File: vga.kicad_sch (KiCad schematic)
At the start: 48 parts

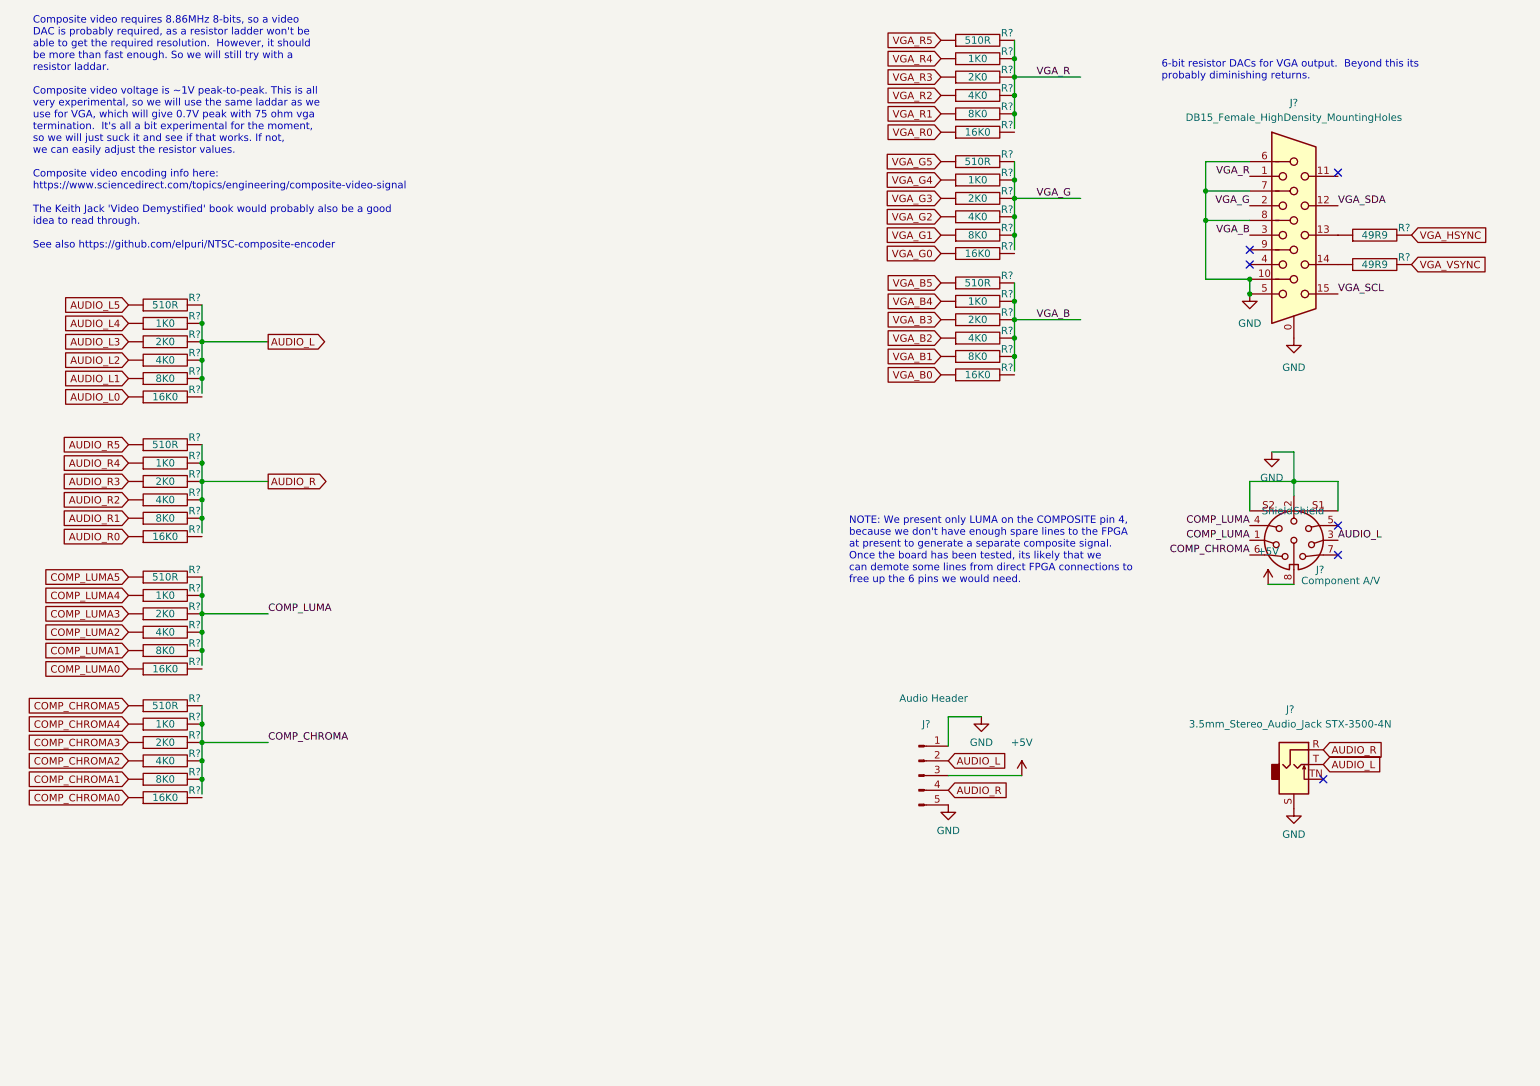
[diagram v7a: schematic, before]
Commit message: beautify the schematics, especially the title-page
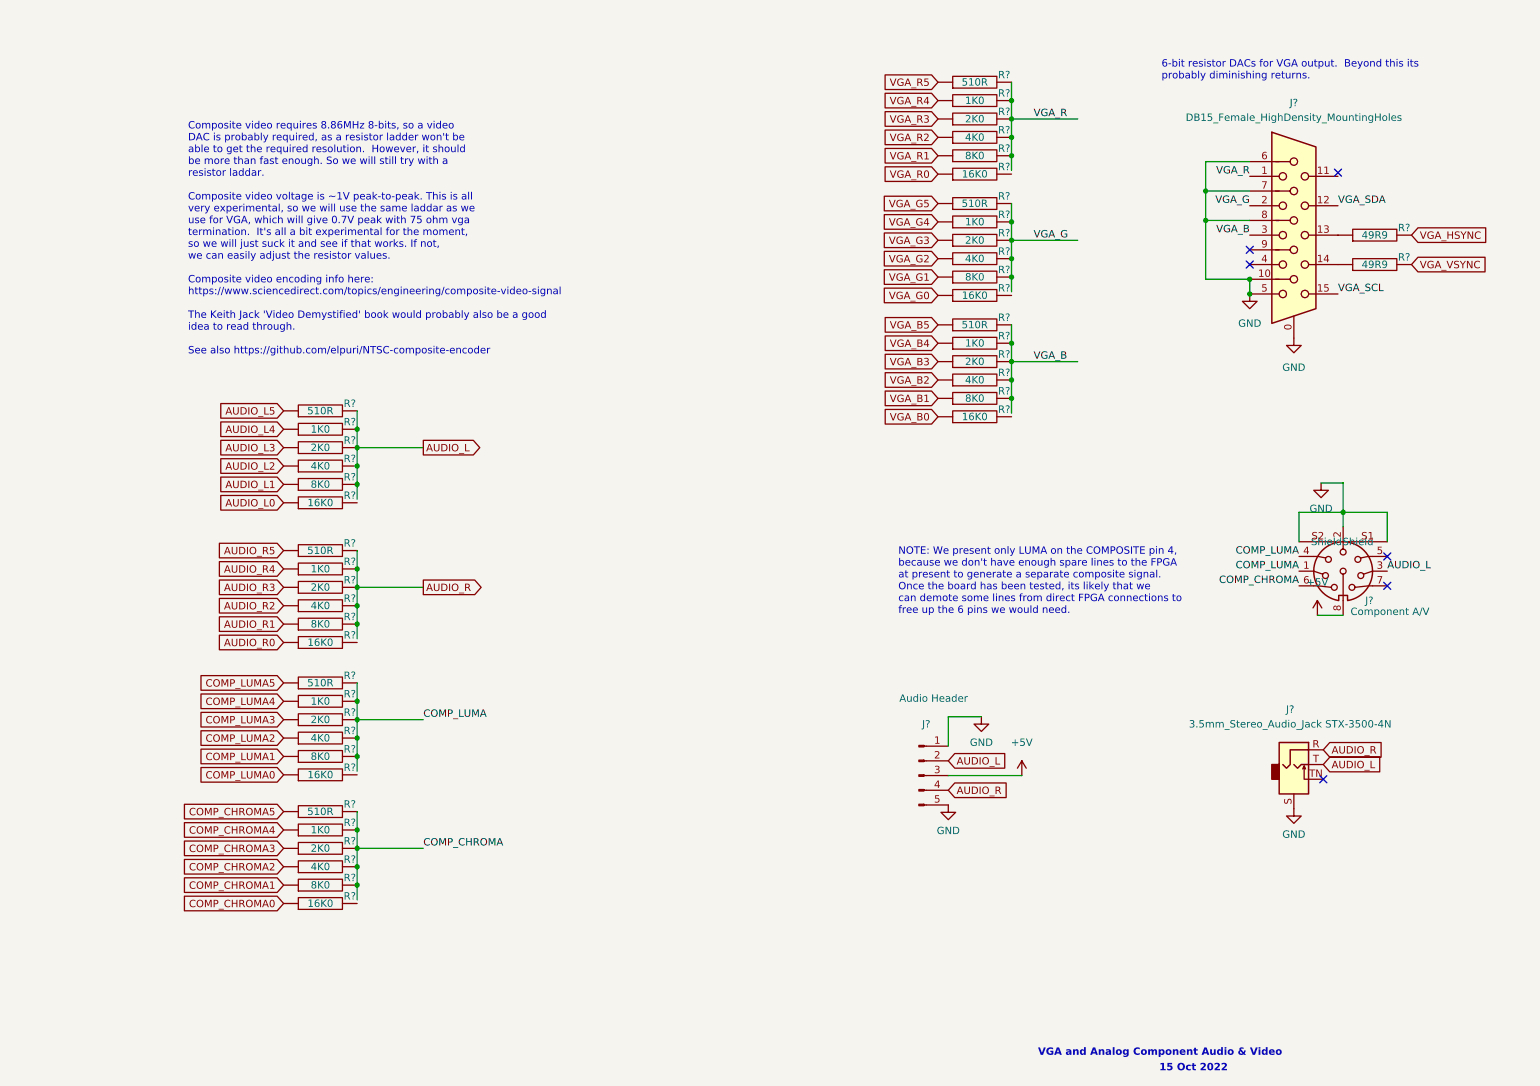
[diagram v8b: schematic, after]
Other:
- note added: "15 Oct 2022"
- note added: "VGA and Analog Component Audio & Video"
- moved on the sheet: J?, R?
